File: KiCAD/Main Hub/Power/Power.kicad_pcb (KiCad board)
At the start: 2 copper layers, 65 x 80 mm, 17 parts, among them J1 Screw_Terminal_01x02, J2 Conn_01x08_Pin, J3 Conn_01x08_Pin, J4 Conn_01x08_Pin, J5 Conn_01x08_Pin, J6 Conn_01x08_Pin, J7 Conn_01x08_Pin

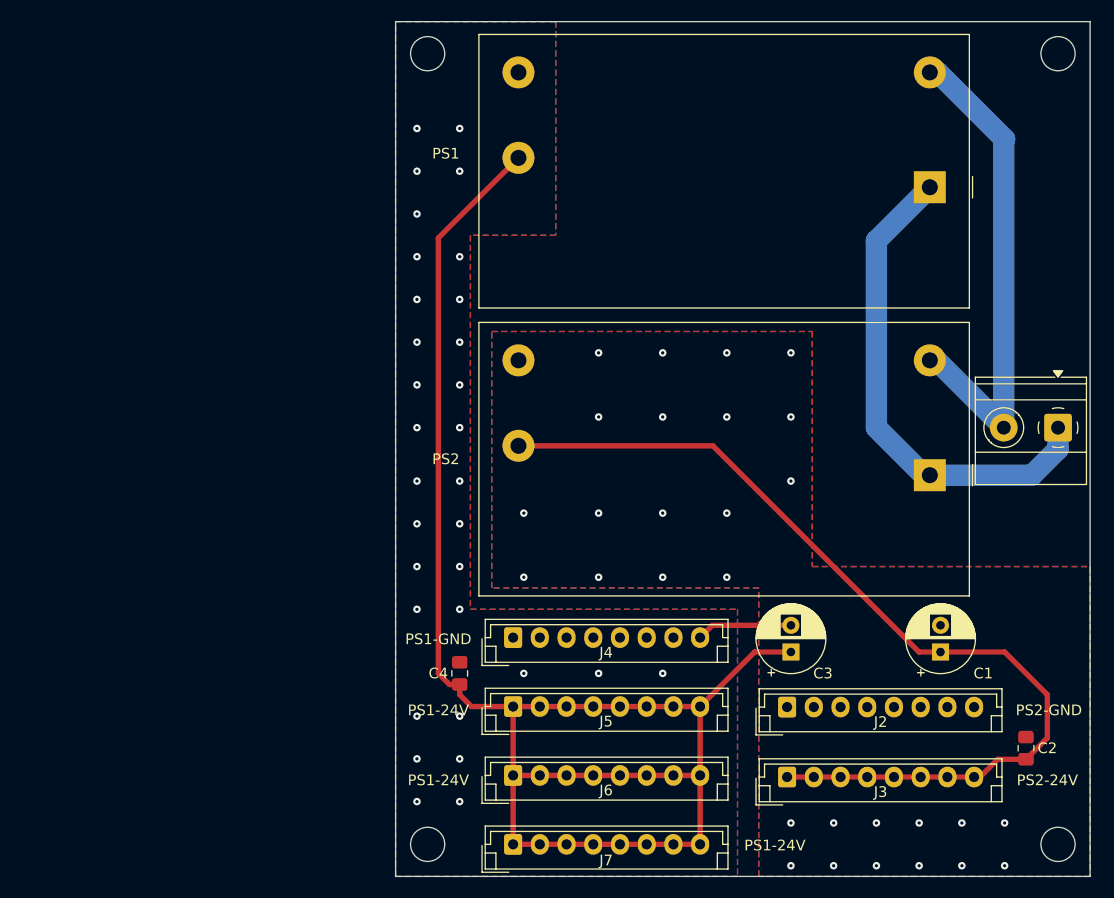
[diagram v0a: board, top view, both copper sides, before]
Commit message: Horizontal power board
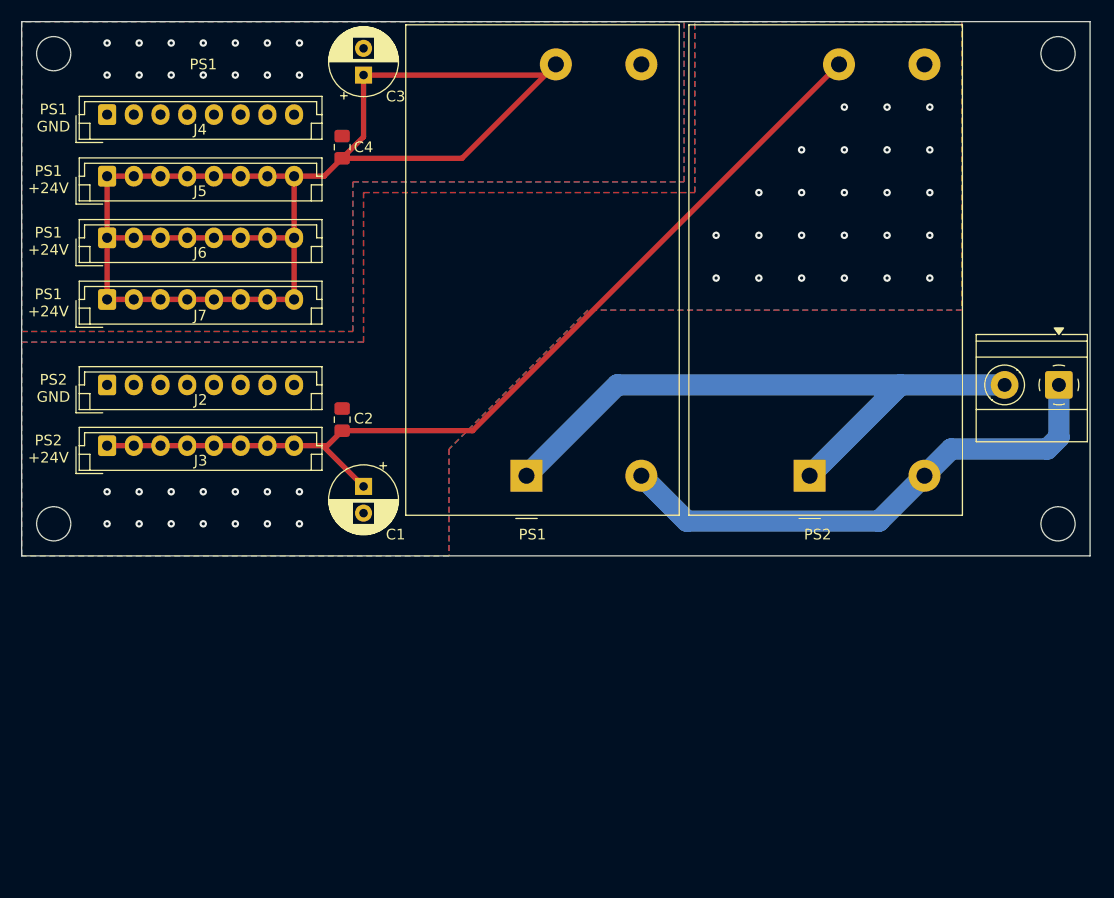
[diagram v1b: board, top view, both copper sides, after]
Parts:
- moved C2 71.0 mm to (80.0, 87.2)
- moved J3 70.8 mm to (58.0, 89.7)
- moved J2 70.4 mm to (58.0, 84.0)
- moved C3 67.2 mm to (82.0, 55.0)
- moved J7 63.6 mm to (58.0, 76.0)
- moved J6 63.1 mm to (58.0, 70.2)
- moved J5 62.5 mm to (58.0, 64.5)
- moved J4 62.0 mm to (58.0, 58.7)
- moved C1 56.2 mm to (82.0, 93.5), turned to -90 degrees
- moved C4 50.5 mm to (80.0, 61.8)
- moved PS1 46.4 mm to (97.2, 92.5), turned to 90 degrees
- moved H4 46.1 mm to (53.0, 97.0)
- moved H1 35.0 mm to (53.0, 53.0)
- moved H3 30.0 mm to (147.0, 97.0)
- moved PS2 11.3 mm to (123.8, 92.5), turned to 90 degrees
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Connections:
- J1 pad 1: VAC -> AC
- J1 pad 2: AC -> VAC
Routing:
- net +24V: track 149.1 -> 130.0 mm
- net VAC: track 46.4 -> 60.3 mm
- net GND2: track 8.98 -> 0.00 mm, vias 32 -> 14
- net AC: track 46.2 -> 49.0 mm
- net +12V: track 89.2 -> 88.7 mm
- net GND: vias 29 -> 38
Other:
- board size 65 x 80 mm -> 100 x 50 mm
- board text added: "PS1"
- board text added: "PS1 +24V"
- board text added: "PS1 GND"
- board text added: "PS2 +24V"
- board text added: "PS2 GND"
- board text removed: "PS1-24V"
- board text removed: "PS1-GND"
- board text removed: "PS2-24V"
- board text removed: "PS2-GND"
